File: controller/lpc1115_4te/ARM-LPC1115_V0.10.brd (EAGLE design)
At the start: 66 x 57.9 mm, 53 parts, among them IC1 LPC1115, IC2 MC34063AP, IC3 MCP1702-33, Q1 BC557B, Q3 BC640C, Q4 12MHz, T1 BC547C

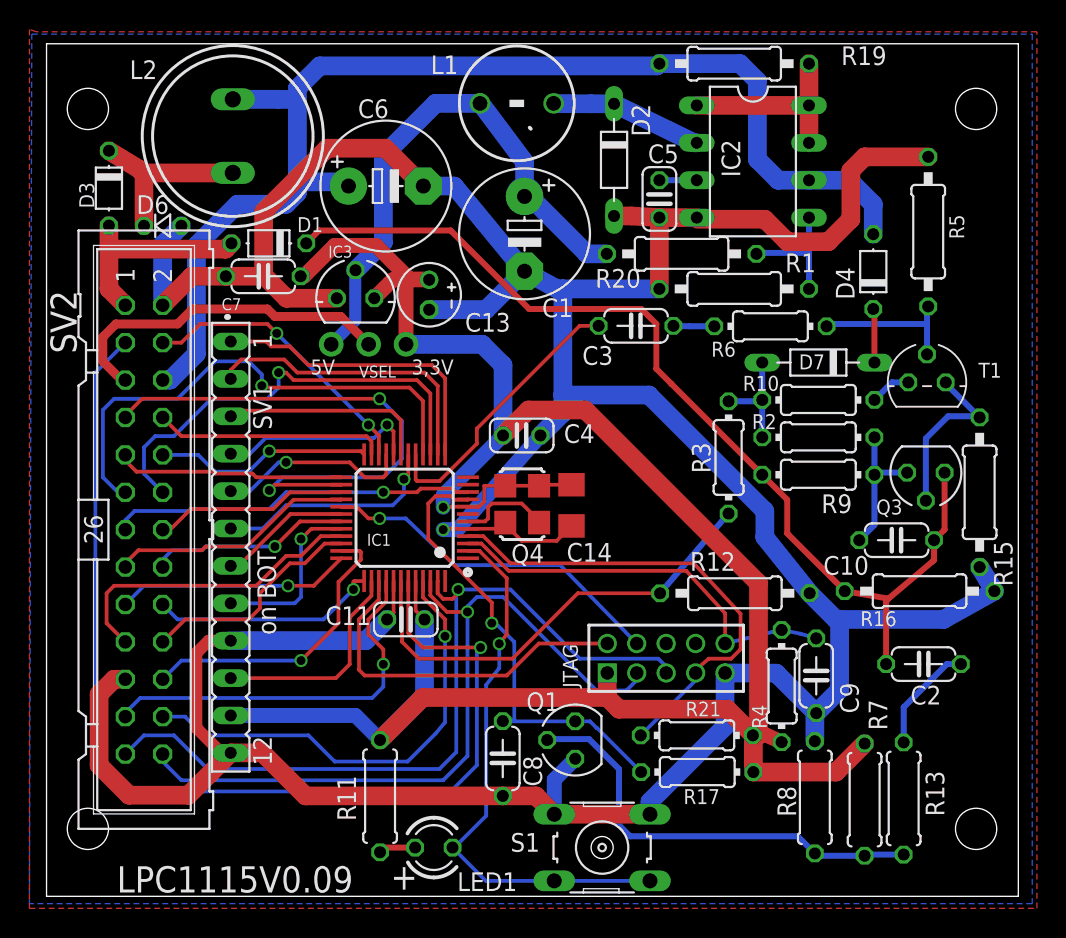
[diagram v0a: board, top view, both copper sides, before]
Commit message: Small layout changes
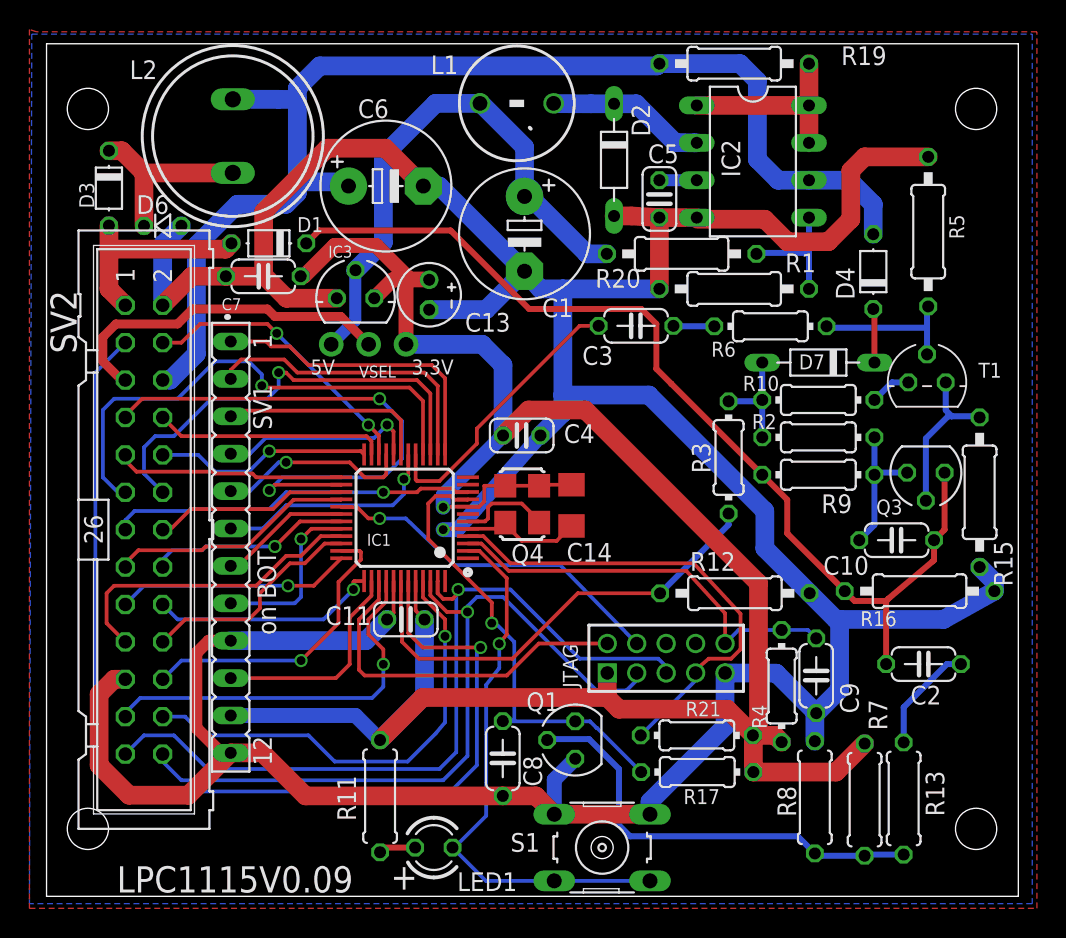
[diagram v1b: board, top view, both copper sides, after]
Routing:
- net N$7: track 11.9 -> 11.0 mm
